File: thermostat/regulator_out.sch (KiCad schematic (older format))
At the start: 28 parts, among them J3 Thermosthat - Molex PicoBlade, J6 Conn_02x02_Odd_Even, Q2 BSS806NL6327, Q6 BSS806NL6327, U5 LM2574M-5, U6 LD1117S33TR_SOT223, U7 LM358

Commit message: Finished layouting tempsensor and thermostat. Parts are ordered from Mouser, PCB ordered from beta-layout.
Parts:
- J3: footprint Connector_Molex:Molex_PicoBlade_53048-0310_1x03_P1.25mm_Horizontal -> Connector_PinHeader_2.54mm:PinHeader_1x03_P2.54mm_Vertical_SMD_Pin1Left
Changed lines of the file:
@@
 F 0 "J3" H 1830 1142 50  0000 L CNN
 F 1 "Thermosthat - Molex PicoBlade" H 1830 1051 50  0000 L CNN
-F 2 "Connector_Molex:Molex_PicoBlade_53048-0310_1x03_P1.25mm_Horizontal" H 1750 1100 50  0001 C CNN
+F 2 "Connector_PinHeader_2.54mm:PinHeader_1x03_P2.54mm_Vertical_SMD_Pin1Left" H 1750 1100 50  0001 C CNN
 F 3 "Molex PicoBlade" H 1750 1100 50  0001 C CNN
 	1    1750 1100

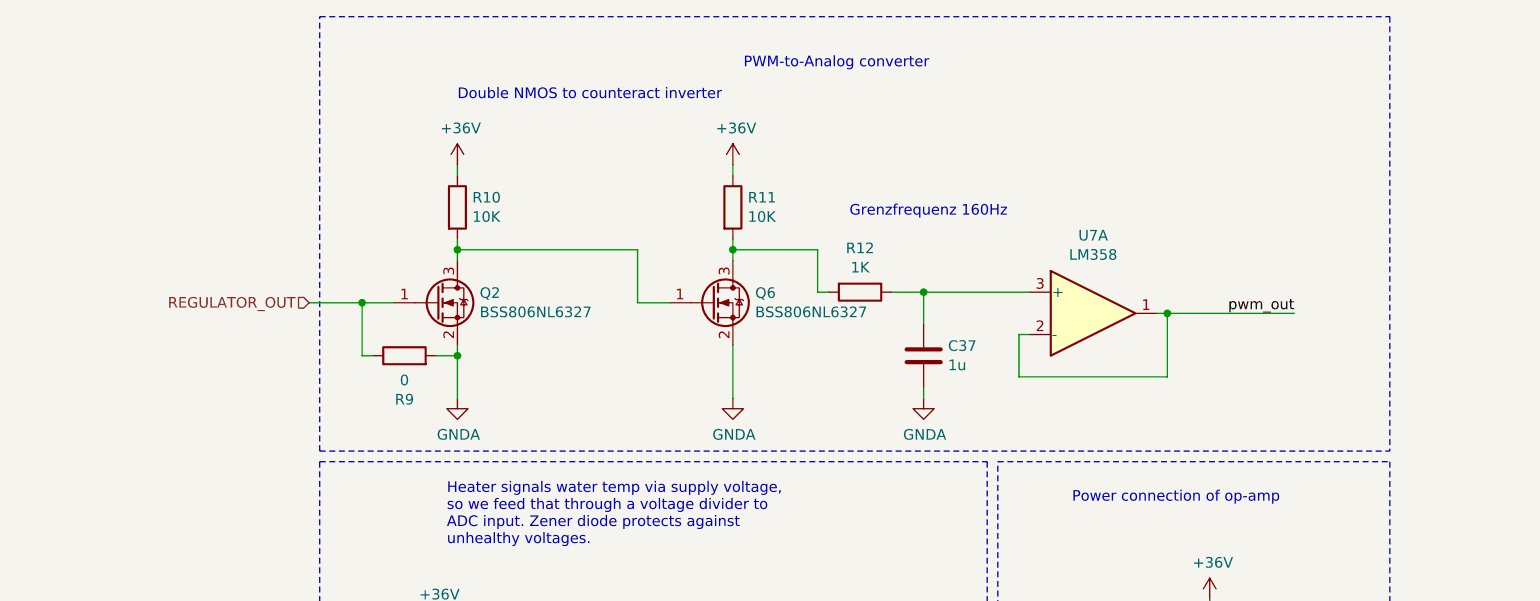
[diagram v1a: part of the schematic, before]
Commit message: Removed pulldown resistor on regulator out pin of MCU. This pin is default non-maskable interrupt pin. On reset, this pulldown resistor immediately triggered the NMI interrupt, sabotaging the startup.
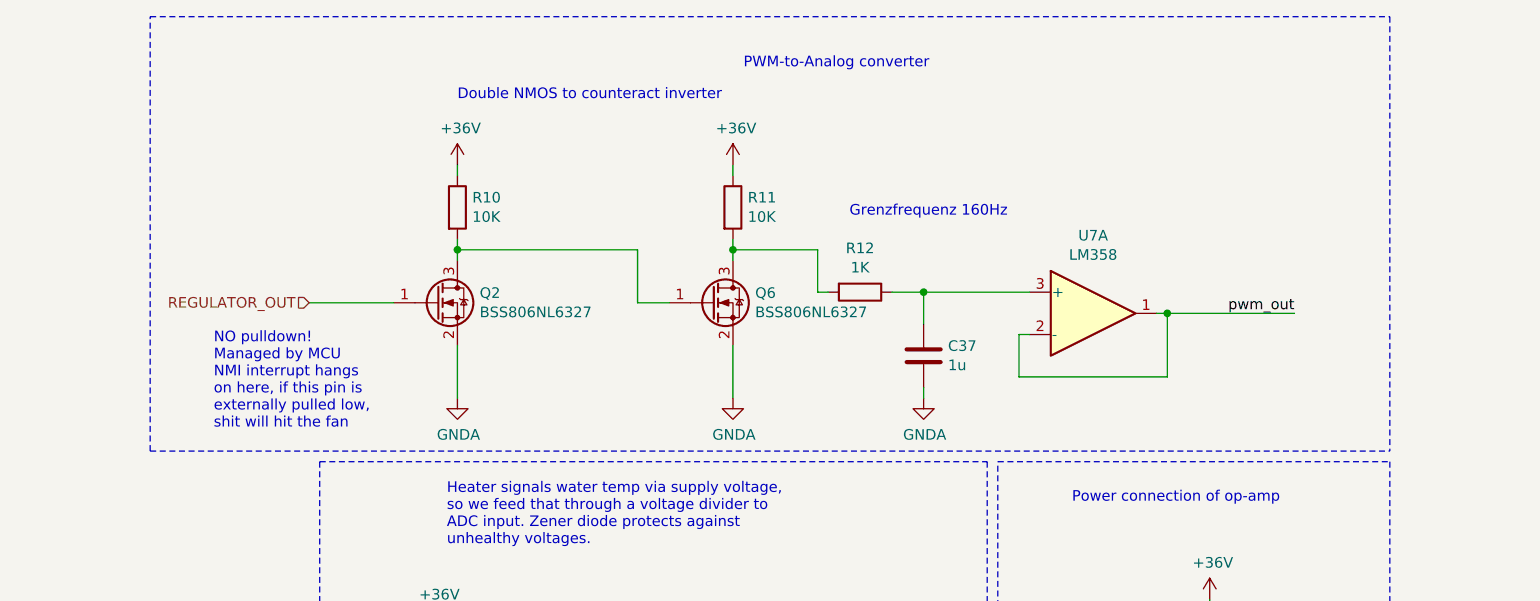
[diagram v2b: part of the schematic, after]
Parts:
- removed R9: 0, Resistor_SMD:R_0603_1608Metric, symbol Device:R
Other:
- note added: "NO pulldown!\nManaged by MCU\nNMI interrupt hangs \non here, if this pin is \nexternally pulled low, \nshit will hit the fan"
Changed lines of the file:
@@
 Grenzfrequenz 160Hz
 Wire Notes Line
-	6100 2650 11150 2650
-Wire Notes Line
 	11150 600  11150 2650
 Wire Notes Line
-	6100 600  11150 600
-Wire Notes Line
-	6100 2650 6100 600
+	5300 2650 5300 600
 Wire Wire Line
 	8050 1300 8050 1350
@@
 Wire Wire Line
 	8050 1650 8050 1700
-Wire Wire Line
-	6750 2400 6750 2200
 $Comp
 L power:GNDA #PWR068
@@
 	8650 4000 8600 4000
 Connection ~ 8600 4000
-$Comp
-L Device:R R9
-U 1 1 5E6AA7AC
-P 6500 2200
-F 0 "R9" V 6293 2200 50  0000 C CNN
-F 1 "0" V 6384 2200 50  0000 C CNN
-F 2 "Resistor_SMD:R_0603_1608Metric" V 6430 2200 50  0001 C CNN
-F 3 "~" H 6500 2200 50  0001 C CNN
-	1    6500 2200
-	0    -1   -1   0
-$EndComp
 Text HLabel 6050 1950 0    50   Input ~ 0
 REGULATOR_OUT
@@
 	1    0    0    -1
 $EndComp
-Wire Wire Line
-	6650 2200 6750 2200
-Connection ~ 6750 2200
-Wire Wire Line
-	6750 2200 6750 2150
-Wire Wire Line
-	6050 1950 6300 1950
-Wire Wire Line
-	6350 2200 6300 2200
-Wire Wire Line
-	6300 2200 6300 1950
-Connection ~ 6300 1950
-Wire Wire Line
-	6300 1950 6450 1950
 $Comp
 L Device:Q_NMOS_GSD Q?
@@
 Wire Wire Line
 	8050 2150 8050 2400
+Text Notes 5600 2550 0    50   ~ 0
+NO pulldown!\nManaged by MCU\nNMI interrupt hangs \non here, if this pin is \nexternally pulled low, \nshit will hit the fan
+Wire Wire Line
+	6750 2150 6750 2400
+Wire Wire Line
+	6050 1950 6450 1950
+Wire Notes Line
+	5300 600  11150 600
+Wire Notes Line
+	5300 2650 11150 2650
 $EndSCHEMATC
